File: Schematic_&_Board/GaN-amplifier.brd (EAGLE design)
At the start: 120.7 x 50.8 mm, 109 parts, among them IC1 LT3080, J1 JOHNSON_SMA_EDGE_LAUNCH_142-0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, J2 JOHNSON_SMA_EDGE_LAUNCH_142-0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, Q1 MMBT3906LT1SMD, T1 IPB080N03L G, T2 IPB080N03L G, T3 IPB080N03L G, T4 IPB080N03L G, T5 BSP89, U1 TPS7A30XX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

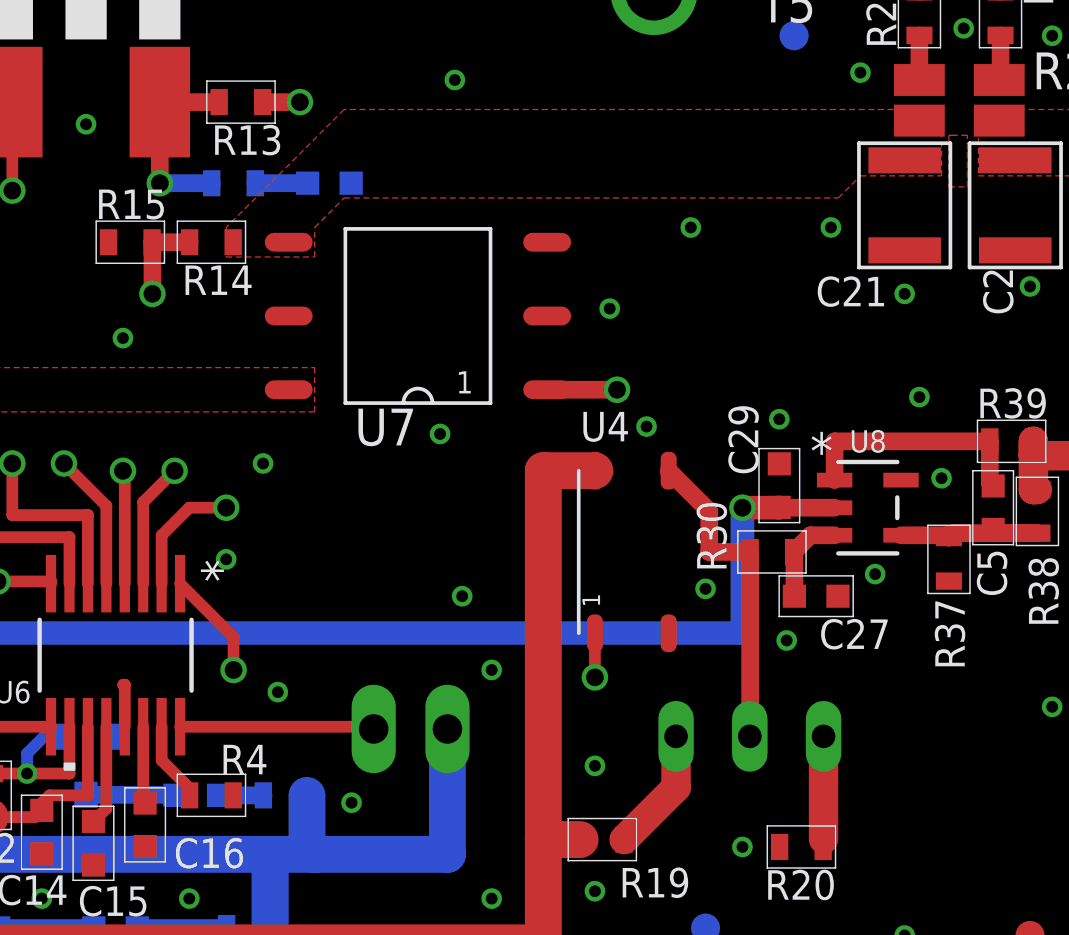
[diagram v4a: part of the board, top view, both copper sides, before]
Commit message: Updates per test board
Adding pulldown on Vdd and On/Off to prevent errors during power
sequencing. Also increasing capacitance of AC coupling capacitors for
better low frequency performance. A couple cosmetic changes to make
component labels visible.

DSB
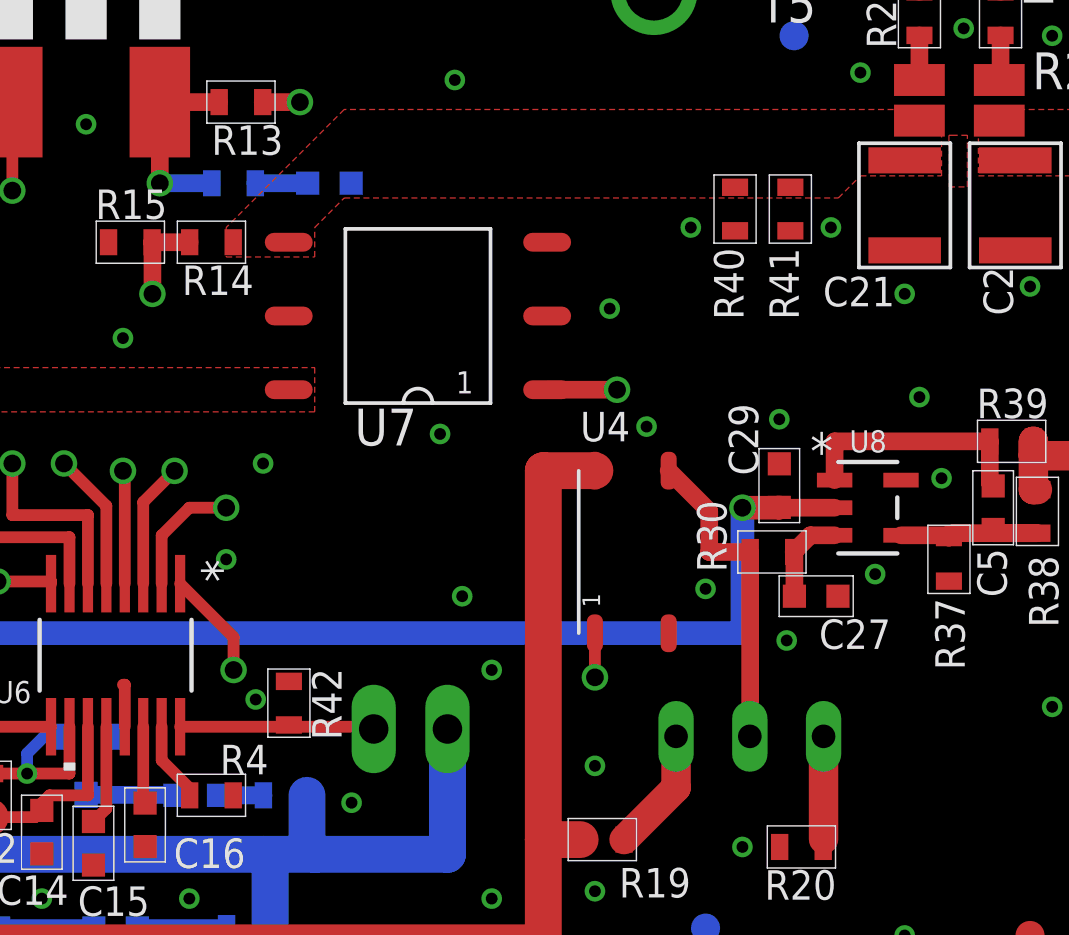
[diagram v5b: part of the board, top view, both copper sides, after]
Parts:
- added R40, R41, R42: 10k, jqi_passives:R_0603
- C15: value 220n -> 1u
- C16: value 150n -> 680n
- C23, C24, C6, C7: value 2.2n -> 22n
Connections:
- net GND: now also R40.P$1, R41.P$1, R42.P$1
- net N$4: now also R42.P$2
- net VDD: now also R40.P$2, R41.P$2
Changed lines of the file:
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@@
 <text x="60.452" y="4.318" size="0.635" layer="22" rot="MR0">No Fault</text>
 <text x="65.024" y="9.144" size="0.635" layer="22" rot="MR0">Sequencing</text>
-<text x="11.938" y="23.368" size="1.016" layer="22" rot="MR90">+24V</text>
-<text x="2.54" y="23.622" size="1.016" layer="22" rot="MR90">-24V</text>
-<text x="9.144" y="27.432" size="1.016" layer="22" rot="MR0">GND</text>
-<text x="71.882" y="7.112" size="1.016" layer="22" rot="MR0">On/Off</text>
-<text x="36.83" y="28.702" size="0.762" layer="22" rot="MR0">RF enable</text>
+<text x="12.446" y="23.368" size="1.016" layer="22" rot="MR90">+24V</text>
+<text x="2.032" y="23.622" size="1.016" layer="22" rot="MR90">-24V</text>
+<text x="9.144" y="28.956" size="1.016" layer="22" rot="MR0">GND</text>
+<text x="72.39" y="5.334" size="1.016" layer="22" rot="MR0">On/Off</text>
+<text x="36.83" y="29.972" size="0.762" layer="22" rot="MR0">RF enable</text>
 <text x="79.756" y="32.004" size="1.016" layer="22" rot="MR0">Idd Monitor</text>
-<text x="74.676" y="5.334" size="0.635" layer="22" rot="MR0">connect to front
+<text x="73.406" y="3.302" size="0.635" layer="22" rot="MR0">connect to front
 rocker switch</text>
 <text x="87.376" y="15.494" size="1.016" layer="22" rot="MR90">Install heatsink on pad</text>
@@
 <attribute name="NAME" x="96.95" y="26.076" size="1.016" layer="25" font="vector" rot="R270"/>
 </element>
-<element name="C6" library="jqi_passives" package="C_MLCC_0603" value="2.2n" x="100.838" y="28.956" smashed="yes" rot="R270">
-<attribute name="PARTNO" value="CL10B222KB8NNNC" x="100.838" y="28.956" size="1.778" layer="27" rot="R270" display="off"/>
+<element name="C6" library="jqi_passives" package="C_MLCC_0603" value="22n" x="100.838" y="28.956" smashed="yes" rot="R270">
+<attribute name="PARTNO" value="CL10B223KB8NNNC" x="100.838" y="28.956" size="1.778" layer="27" rot="R270" display="off"/>
 <attribute name="NAME" x="100.876" y="27.716" size="1.016" layer="25" font="vector" rot="R270"/>
 </element>
-<element name="C7" library="jqi_passives" package="C_MLCC_0603" value="2.2n" x="100.33" y="20.32" smashed="yes" rot="R90">
-<attribute name="PARTNO" value="CL10B222KB8NNNC" x="100.33" y="20.32" size="1.778" layer="27" rot="R90" display="off"/>
+<element name="C7" library="jqi_passives" package="C_MLCC_0603" value="22n" x="100.33" y="20.32" smashed="yes" rot="R90">
+<attribute name="PARTNO" value="CL10B223KB8NNNC" x="100.33" y="20.32" size="1.778" layer="27" rot="R90" display="off"/>
 <attribute name="NAME" x="101.63" y="18.758" size="1.016" layer="25" font="vector" rot="R180"/>
 </element>
@@
 <attribute name="VALUE" x="71.12" y="6.985" size="1.27" layer="28" rot="MR0"/>
 </element>
-<element name="C15" library="jqi_passives" package="C_MLCC_0603" value="220n" x="57.658" y="6.223" smashed="yes" rot="R270">
+<element name="C15" library="jqi_passives" package="C_MLCC_0603" value="1u" x="57.658" y="6.223" smashed="yes" rot="R270">
 <attribute name="NAME" x="57.12" y="3.721" size="1.016" layer="25" font="vector"/>
-<attribute name="PARTNO" value="CL10B224KP8NNNC" x="57.658" y="6.223" size="1.778" layer="27" rot="R270" display="off"/>
-</element>
-<element name="C16" library="jqi_passives" package="C_MLCC_0603" value="150n" x="59.436" y="6.858" smashed="yes" rot="R270">
+<attribute name="PARTNO" value="CL10B105KA8NNNC" x="57.658" y="6.223" size="1.778" layer="27" rot="R270" display="off"/>
+</element>
+<element name="C16" library="jqi_passives" package="C_MLCC_0603" value="680n" x="59.436" y="6.858" smashed="yes" rot="R270">
 <attribute name="NAME" x="60.422" y="5.372" size="1.016" layer="25" font="vector"/>
-<attribute name="PARTNO" value="CL10B154KP8NNNC" x="59.436" y="6.858" size="1.778" layer="27" rot="R270" display="off"/>
+<attribute name="PARTNO" value="CL10B684KO8NFNC" x="59.436" y="6.858" size="1.778" layer="27" rot="R270" display="off"/>
 </element>
 <element name="R4" library="jqi_passives" package="R_0603" value="49.9k" x="61.722" y="7.874" smashed="yes" rot="R180">
@@
 <attribute name="NAME" x="89.99" y="32.192" size="1.27" layer="25"/>
 </element>
-<element name="C23" library="jqi_passives" package="C_MLCC_0603" value="2.2n" x="105.41" y="45.466" smashed="yes" rot="R270">
-<attribute name="PARTNO" value="CL10B222KB8NNNC" x="105.41" y="45.466" size="1.778" layer="27" rot="R270" display="off"/>
+<element name="C23" library="jqi_passives" package="C_MLCC_0603" value="22n" x="105.41" y="45.466" smashed="yes" rot="R270">
+<attribute name="PARTNO" value="CL10B223KB8NNNC" x="105.41" y="45.466" size="1.778" layer="27" rot="R270" display="off"/>
 <attribute name="NAME" x="106.904" y="44.488" size="1.016" layer="25" font="vector"/>
 </element>
-<element name="C24" library="jqi_passives" package="C_MLCC_0603" value="2.2n" x="105.41" y="5.334" smashed="yes" rot="R270">
-<attribute name="PARTNO" value="CL10B222KB8NNNC" x="105.41" y="5.334" size="1.778" layer="27" rot="R270" display="off"/>
+<element name="C24" library="jqi_passives" package="C_MLCC_0603" value="22n" x="105.41" y="5.334" smashed="yes" rot="R270">
+<attribute name="PARTNO" value="CL10B223KB8NNNC" x="105.41" y="5.334" size="1.778" layer="27" rot="R270" display="off"/>
 <attribute name="NAME" x="106.904" y="6.134" size="1.016" layer="25" font="vector"/>
 </element>
@@
 <element name="C21" library="jqi_passives" package="C_MLCC_1210" value="10u" x="85.598" y="28.194" smashed="yes" rot="R90">
 <attribute name="PARTNO" value="UMK325C7106MM-T" x="85.598" y="28.194" size="1.778" layer="27" rot="R90" display="off"/>
-<attribute name="NAME" x="85.004" y="25.732" size="1.016" layer="25" font="vector" rot="R180"/>
+<attribute name="NAME" x="85.258" y="25.732" size="1.016" layer="25" font="vector" rot="R180"/>
 </element>
 <element name="FID5" library="fiducials-jqi" package="FID_1.0MM" value="FIDUCIAL-1.0MM" x="4.826" y="30.734" rot="MR0"/>
@@
 <attribute name="PARTNO" value="CL10B104KB8SFNC" x="82.55" y="14.732" size="1.778" layer="27" rot="R180" display="off"/>
 <attribute name="NAME" x="85.12" y="13.932" size="1.016" layer="25" font="vector" rot="R180"/>
+</element>
+<element name="R40" library="jqi_passives" package="R_0603" value="10k" x="79.756" y="28.067" smashed="yes" rot="R90">
+<attribute name="PARTNO" value="ERJ-3EKF1002V" x="79.756" y="28.067" size="1.778" layer="27" rot="R90" display="off"/>
+<attribute name="NAME" x="79.032" y="26.727" size="1.016" layer="25" font="vector" rot="R270"/>
+</element>
+<element name="R41" library="jqi_passives" package="R_0603" value="10k" x="81.661" y="28.067" smashed="yes" rot="R90">
+<attribute name="PARTNO" value="ERJ-3EKF1002V" x="81.661" y="28.067" size="1.778" layer="27" rot="R90" display="off"/>
+<attribute name="NAME" x="80.937" y="26.727" size="1.016" layer="25" font="vector" rot="R270"/>
+</element>
+<element name="R42" library="jqi_passives" package="R_0603" value="10k" x="64.389" y="11.049" rot="R270">
+<attribute name="PARTNO" value="ERJ-3EKF1002V" x="64.389" y="11.049" size="1.778" layer="27" rot="R270" display="off"/>
 </element>
 </elements>
@@
 <via x="53.086" y="19.812" extent="1-16" drill="0.4064"/>
 <via x="63.5" y="19.304" extent="1-16" drill="0.4064"/>
-<via x="64.008" y="11.43" extent="1-16" drill="0.4064"/>
+<via x="63.246" y="11.176" extent="1-16" drill="0.4064"/>
 <via x="51.816" y="9.906" extent="1-16" drill="0.4064"/>
 <via x="44.958" y="18.796" extent="1-16" drill="0.4064"/>
@@
 <via x="86.106" y="21.59" extent="1-16" drill="0.4064"/>
 <via x="81.534" y="13.208" extent="1-16" drill="0.4064"/>
+<contactref element="R42" pad="P$1"/>
+<contactref element="R40" pad="P$1"/>
+<contactref element="R41" pad="P$1"/>
 </signal>
 <signal name="N$15">
@@
 <contactref element="JP1" pad="2"/>
 <contactref element="U6" pad="16"/>
-<wire x1="60.6425" y1="10.2362" x2="67.2338" y2="10.2362" width="0.4064" layer="1"/>
+<wire x1="60.6425" y1="10.2362" x2="64.389" y2="10.2362" width="0.4064" layer="1"/>
+<wire x1="65.278" y1="10.2362" x2="67.2338" y2="10.2362" width="0.4064" layer="1"/>
 <wire x1="67.2338" y1="10.2362" x2="67.31" y2="10.16" width="0.4064" layer="1"/>
+<contactref element="R42" pad="P$2"/>
+<wire x1="64.389" y1="10.299" x2="64.389" y2="10.2362" width="0.4064" layer="1"/>
+<wire x1="64.389" y1="10.2362" x2="65.278" y2="10.2362" width="0.4064" layer="1"/>
 </signal>
 <signal name="*FAULT">
@@
 </polygon>
 <contactref element="C21" pad="P$2"/>
+<contactref element="R40" pad="P$2"/>
+<contactref element="R41" pad="P$2"/>
 </signal>
 <signal name="N$14">

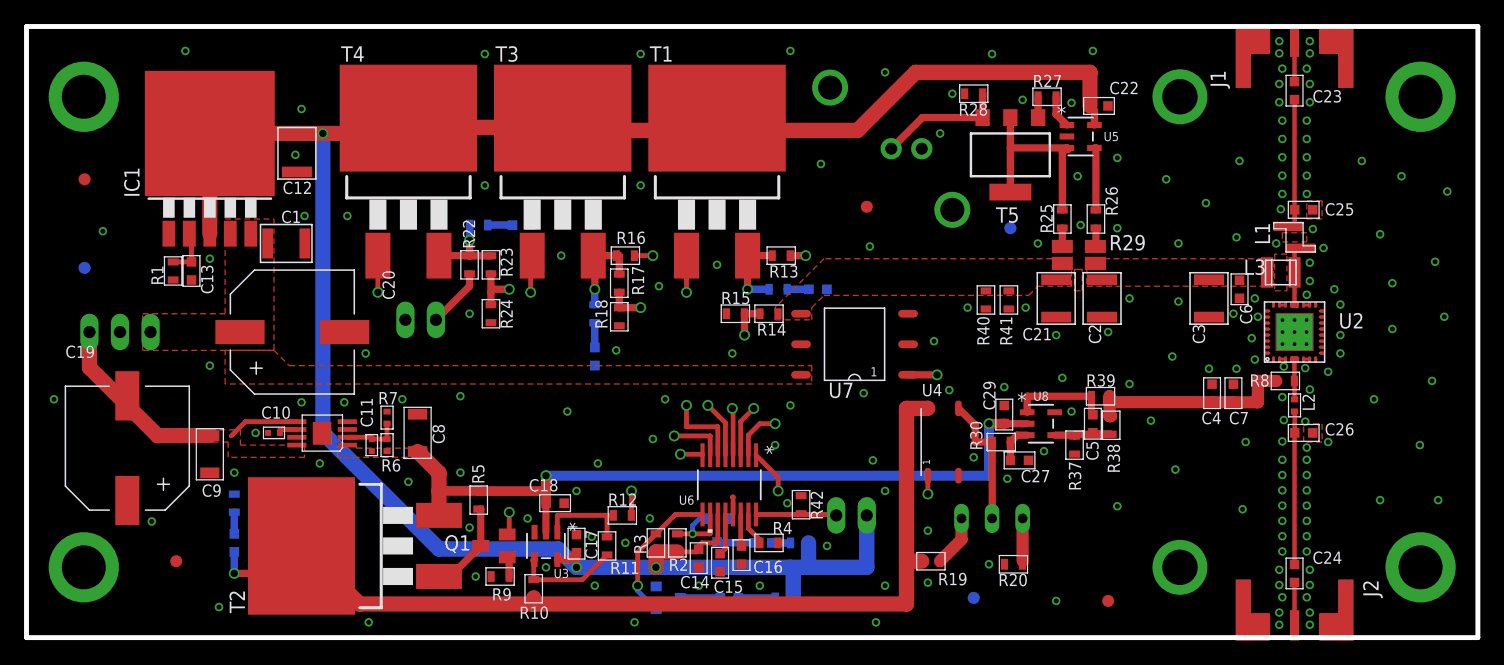
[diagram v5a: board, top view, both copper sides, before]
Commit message: More test board updates
Adjusted fiducial position per Zach's advice and added switch debouncing
components.

DSB
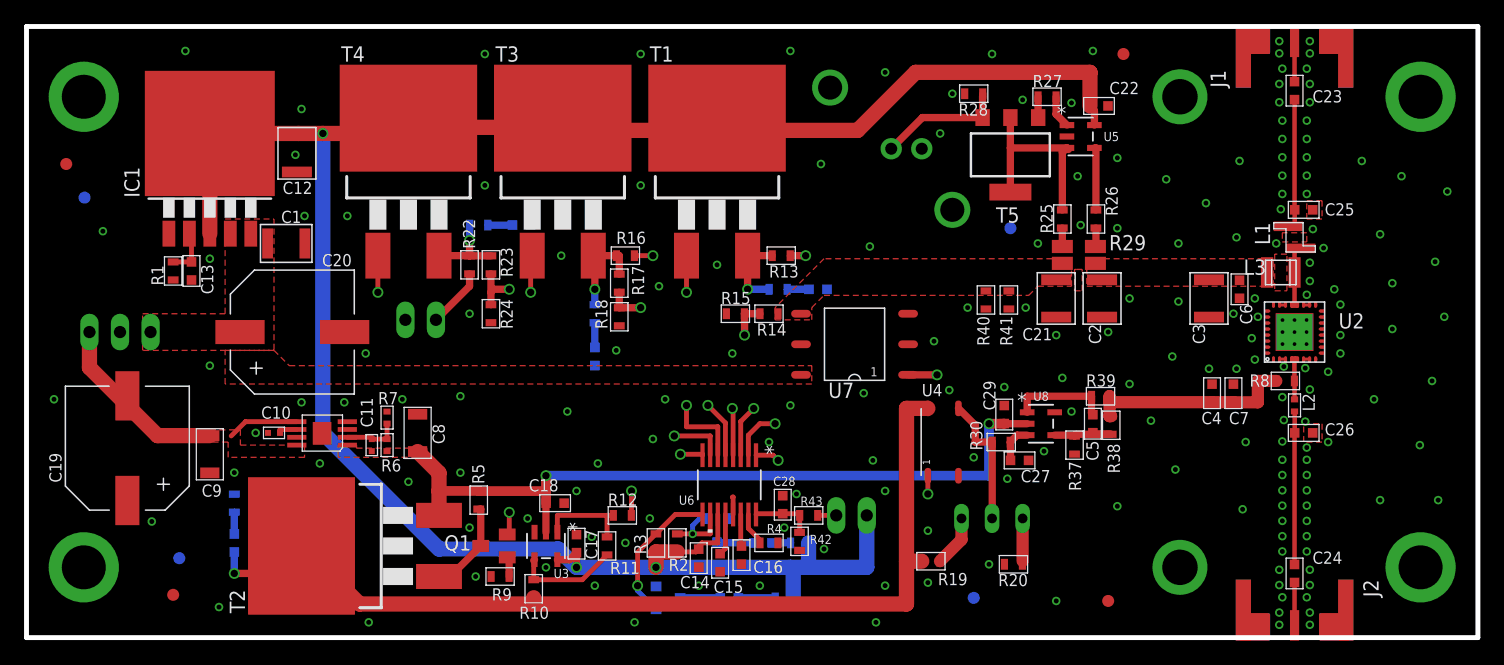
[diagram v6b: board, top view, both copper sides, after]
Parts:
- added C28: 680n, jqi_passives:C_MLCC_0603
- added R43: 1k, jqi_passives:R_0603
- C18, C22: value 0.1u -> 100n
- moved FID3 24.8 mm to (91.2, 48.5)
- moved FID6 10.2 mm to (12.7, 6.60)
- moved FID5 5.84 mm to (4.83, 36.6)
- moved R42 3.05 mm to (64.3, 8.00), turned to 90 degrees
- moved FID1 2.81 mm to (12.2, 3.56)
- moved FID2 1.98 mm to (3.30, 39.4)
- turned JP3 to 180 degrees
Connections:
- new net N$44: C28.P$1, R42.P$2, R43.P$2, U6.16
- net +24V: now also JP3.3; no longer JP3.1
- net -24V: now also JP3.1; no longer JP3.3
- net GND: now also C28.P$2
- net N$4: now also R43.P$1; no longer R42.P$2, U6.16
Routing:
- net N$4: track 6.76 -> 1.54 mm
- net N$44: track 0.00 -> 5.13 mm
- net VPIN_DET: track 18.0 -> 17.3 mm
- net GND: vias 193 -> 194

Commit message: Changed coupling caps
I changed the RF coupling capacitors to a lower ESR component. We should
consider an ultra-broadband cap also, but the expense seems excessive.

DSB
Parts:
- C23, C24: value 22n -> 10n
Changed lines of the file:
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@@
 <attribute name="NAME" x="89.99" y="32.192" size="1.27" layer="25"/>
 </element>
-<element name="C23" library="jqi_passives" package="C_MLCC_0603" value="22n" x="105.41" y="45.466" smashed="yes" rot="R270">
-<attribute name="PARTNO" value="CL10B223KB8NNNC" x="105.41" y="45.466" size="1.778" layer="27" rot="R270" display="off"/>
+<element name="C23" library="jqi_passives" package="C_MLCC_0603" value="10n" x="105.41" y="45.466" smashed="yes" rot="R270">
+<attribute name="PARTNO" value="CL10B103KB8NCNC" x="105.41" y="45.466" size="1.778" layer="27" rot="R270" display="off"/>
 <attribute name="NAME" x="106.904" y="44.488" size="1.016" layer="25" font="vector"/>
 </element>
-<element name="C24" library="jqi_passives" package="C_MLCC_0603" value="22n" x="105.41" y="5.334" smashed="yes" rot="R270">
-<attribute name="PARTNO" value="CL10B223KB8NNNC" x="105.41" y="5.334" size="1.778" layer="27" rot="R270" display="off"/>
+<element name="C24" library="jqi_passives" package="C_MLCC_0603" value="10n" x="105.41" y="5.334" smashed="yes" rot="R270">
+<attribute name="PARTNO" value="CL10B103KB8NCNC" x="105.41" y="5.334" size="1.778" layer="27" rot="R270" display="off"/>
 <attribute name="NAME" x="106.904" y="6.134" size="1.016" layer="25" font="vector"/>
 </element>
